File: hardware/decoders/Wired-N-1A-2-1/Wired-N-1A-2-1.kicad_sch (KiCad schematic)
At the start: 37 parts, among them J1 CA, J10 RL, J11 RR, J12 FOF, J13 F0R, J14 MCLR, J15 +5, J16 GND, J17 PGD, J18 PGC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

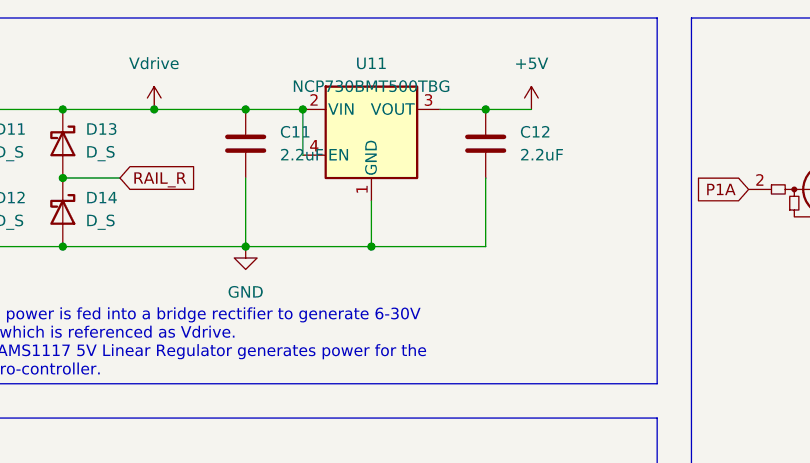
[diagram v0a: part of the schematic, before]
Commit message: Tweaked the board to shave 2mm, now 9mm x 18mm.
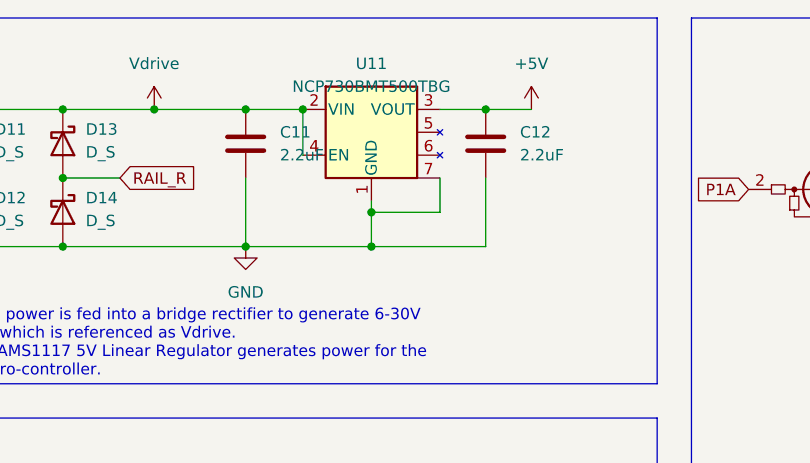
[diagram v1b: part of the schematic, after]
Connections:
- net GND: now also U11.7
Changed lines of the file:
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@@
   (junction (at 66.04 76.2) (diameter 0) (color 0 0 0 0)
   )
+  (junction (at 82.55 36.83) (diameter 0) (color 0 0 0 0)
+  )
   (junction (at 48.26 40.64) (diameter 0) (color 0 0 0 0)
   )
@@
     (stroke (width 0) (type default) (color 0 0 0 0))
   )
-  (wire (pts (xy 82.55 40.64) (xy 82.55 35.56))
+  (wire (pts (xy 82.55 40.64) (xy 82.55 36.83))
     (stroke (width 0) (type default) (color 0 0 0 0))
   )
@@
     (stroke (width 0) (type default) (color 0 0 0 0))
   )
+  (wire (pts (xy 82.55 36.83) (xy 82.55 35.56))
+    (stroke (width 0) (type default) (color 0 0 0 0))
+  )
   (wire (pts (xy 243.84 31.75) (xy 247.65 31.75))
     (stroke (width 0) (type default) (color 0 0 0 0))
@@
     (stroke (width 0) (type default) (color 0 0 0 0))
   )
+  (wire (pts (xy 90.17 36.83) (xy 82.55 36.83))
+    (stroke (width 0) (type default) (color 0 0 0 0))
+  )
   (wire (pts (xy 166.37 46.99) (xy 166.37 49.53))
     (stroke (width 0) (type default) (color 0 0 0 0))
@@
   )
   (wire (pts (xy 194.31 29.21) (xy 198.12 29.21))
+    (stroke (width 0) (type default) (color 0 0 0 0))
+  )
+  (wire (pts (xy 90.17 33.02) (xy 90.17 36.83))
     (stroke (width 0) (type default) (color 0 0 0 0))
   )
@@
       (effects (font (size 1.27 1.27)) hide)
     )
-    (property "Datasheet" "https://datasheet.lcsc.com/lcsc/2108181730_onsemi-NCP730BMT500TBG_C892822.pdf" (id 3) (at 85.09 34.29 0)
+    (property "Datasheet" "https://datasheet.lcsc.com/lcsc/2108181730_onsemi-NCP730BMT500TBG_C892822.pdf" (id 3) (at 85.09 40.64 0)
       (effects (font (size 1.27 1.27)) hide)
     )
@@
       (effects (font (size 1.27 1.27)) hide)
     )
+    (pin "5")
+    (pin "6")
+    (pin "7")
     (pin "1")
     (pin "2")
